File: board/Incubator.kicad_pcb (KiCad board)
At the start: 2 copper layers, 96.5 x 81.3 mm, 53 parts, among them J1 TFT SPI interface, J10 NTC2, J2 I2C connector, J3 DHT11, J4 Relay1, J5 VAC 230V, J6 VDC 5V, J7 Relay2, J8 NTC, J9 TX RX - +, K1 FINDER-36.11, K2 FINDER-36.11, Q1 BC547, Q2 BC547, Q3 BC847, Q4 BC847, U1 ESP32-WROOM-32, U2 MAX485E, U3 AMS1117-3.3

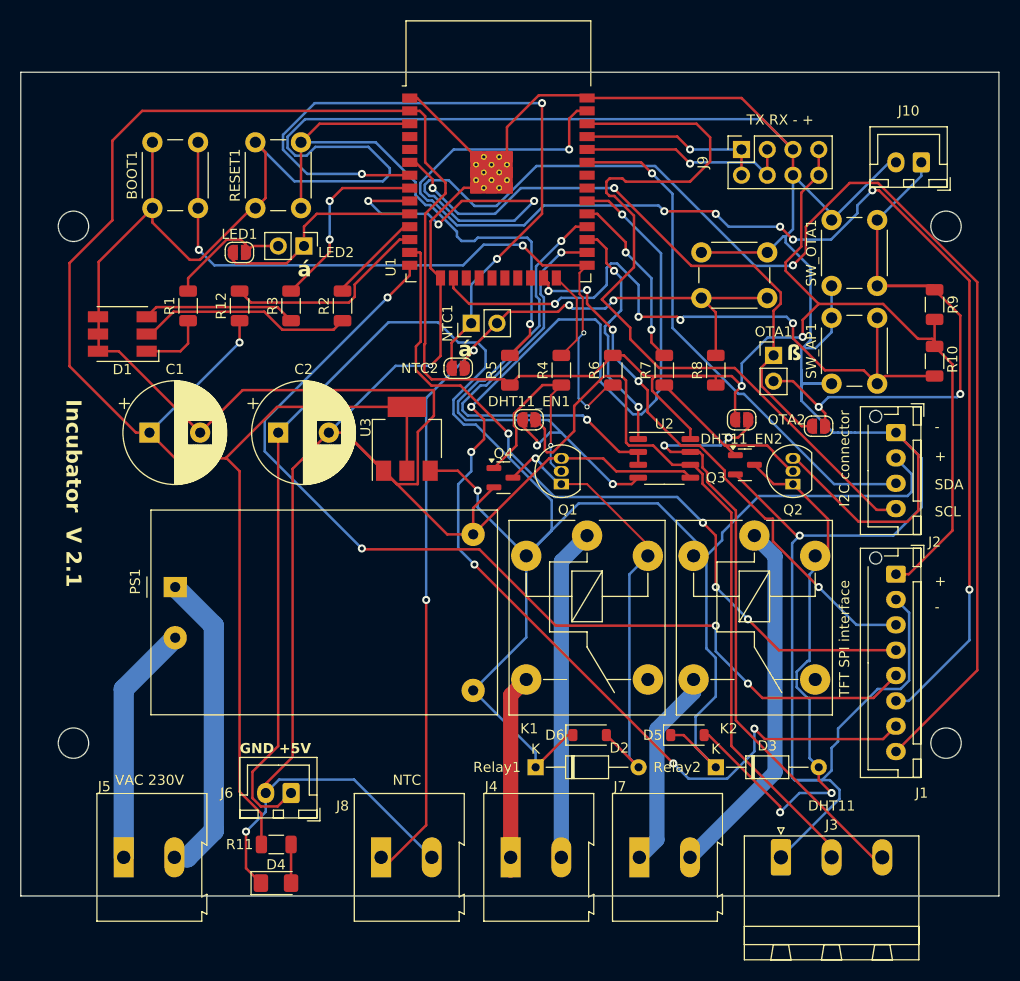
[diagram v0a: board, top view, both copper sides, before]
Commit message: [UPD] Update days and avoid wire interferences
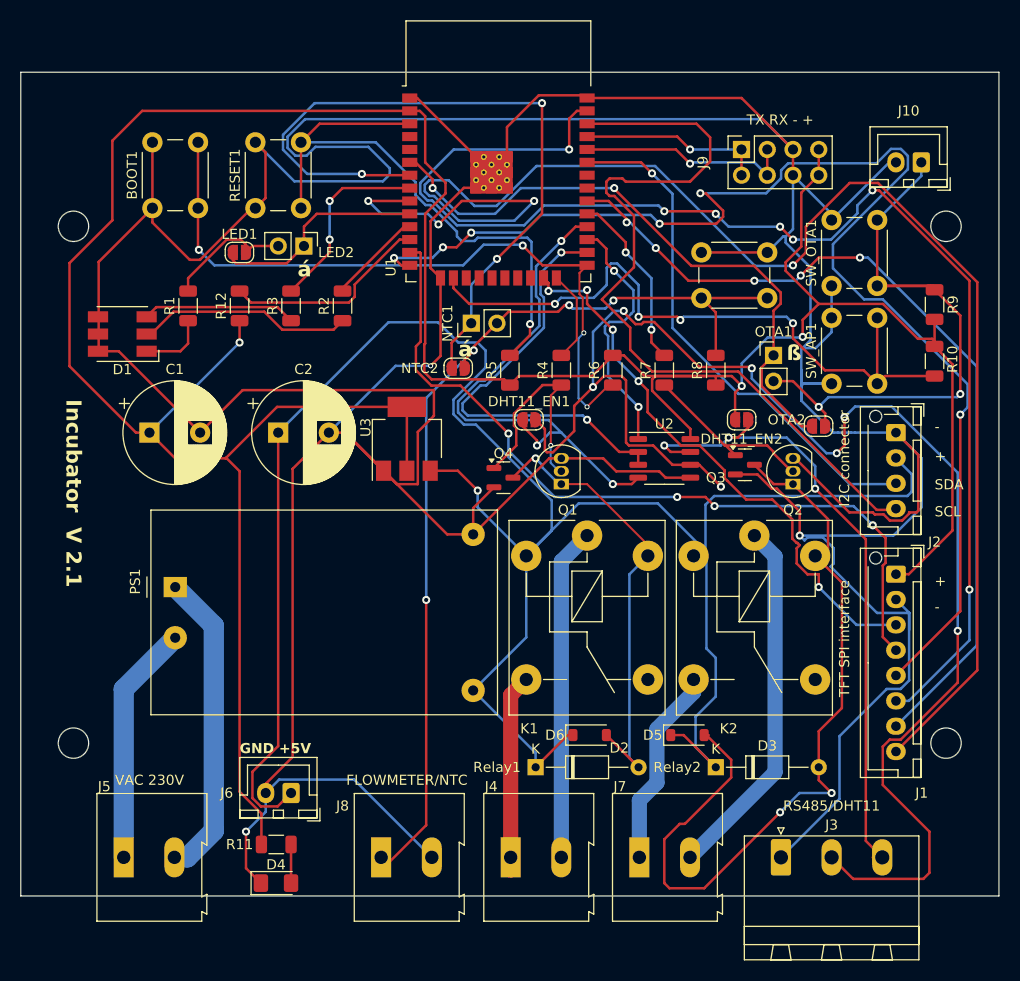
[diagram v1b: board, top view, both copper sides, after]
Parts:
- J3: value DHT11 -> RS485/DHT11
- J8: value NTC -> FLOWMETER/NTC
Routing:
- net Net-(DHT11_EN1-B): track 74.2 -> 145.9 mm, vias 0 -> 7
- net /SPI_SCK: track 126.1 -> 86.1 mm, vias 6 -> 5
- net /SPI_DC: track 100.1 -> 128.3 mm, vias 4 -> 6
- net Net-(D3-A): track 56.3 -> 79.0 mm
- net GND: track 575.7 -> 562.0 mm
- net /SPI_RESET: track 75.6 -> 78.8 mm
- net Net-(DHT11_EN2-B): track 61.6 -> 64.7 mm, vias 2 -> 3
- net +5V: track 218.0 -> 220.6 mm
- net /SPI_CS: track 54.8 -> 56.8 mm
- net Net-(U1-IO16): track 24.0 -> 25.5 mm
- net Net-(J2-Pin_4): track 79.0 -> 79.6 mm
